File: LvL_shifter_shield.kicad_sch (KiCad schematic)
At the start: 10 parts, among them J1 Conn_02x08_Counter_Clockwise, J2 Conn_01x15_Socket, J3 Conn_01x15_Socket, J4 Power, U1 TXB0108DQSR, U2 TXB0108DQSR

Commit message: Updated silkscreen and added a +5 link to the nano
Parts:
- added R3: ${SIM.PARAMS}, Resistor_SMD:R_0603_1608Metric_Pad0.98x0.95mm_HandSolder, symbol Device:R_Small
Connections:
- net +5V: now also R3.2
- net +5V2: now also R3.1
- no-connect marks 11 -> 12
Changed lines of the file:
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@@
   (junction (at 53.34 119.38) (diameter 0) (color 0 0 0 0)
+  )
+  (junction (at 50.8 144.78) (diameter 0) (color 0 0 0 0)
+  )
+  (junction (at 106.68 20.32) (diameter 0) (color 0 0 0 0)
   )
   (junction (at 58.42 77.47) (diameter 0) (color 0 0 0 0)
@@
   (no_connect (at 77.47 147.32))
   (no_connect (at 77.47 139.7))
+  (no_connect (at 109.22 20.32))
   (no_connect (at 77.47 142.24))
   (wire (pts (xy 58.42 138.43) (xy 53.34 138.43))
@@
     (stroke (width 0) (type default))
   )
+  (wire (pts (xy 50.8 144.78) (xy 35.56 144.78))
+    (stroke (width 0) (type default))
+  )
   (wire (pts (xy 132.08 54.61) (xy 175.26 54.61))
     (stroke (width 0) (type default))
@@
     (stroke (width 0) (type default))
   )
+  (wire (pts (xy 35.56 144.78) (xy 35.56 16.51))
+    (stroke (width 0) (type default))
+  )
   (wire (pts (xy 157.48 64.77) (xy 175.26 64.77))
     (stroke (width 0) (type default))
@@
     (stroke (width 0) (type default))
   )
+  (wire (pts (xy 106.68 20.32) (xy 114.3 20.32))
+    (stroke (width 0) (type default))
+  )
   (wire (pts (xy 83.82 121.92) (xy 83.82 62.23))
     (stroke (width 0) (type default))
@@
     (stroke (width 0) (type default))
   )
+  (wire (pts (xy 104.14 15.24) (xy 104.14 16.51))
+    (stroke (width 0) (type default))
+  )
   (wire (pts (xy 101.6 25.4) (xy 101.6 74.93))
     (stroke (width 0) (type default))
@@
     (stroke (width 0) (type default))
   )
+  (wire (pts (xy 35.56 16.51) (xy 104.14 16.51))
+    (stroke (width 0) (type default))
+  )
   (wire (pts (xy 105.41 40.64) (xy 105.41 41.91))
     (stroke (width 0) (type default))
@@
     (stroke (width 0) (type default))
   )
-  (wire (pts (xy 101.6 20.32) (xy 114.3 20.32))
+  (wire (pts (xy 101.6 20.32) (xy 106.68 20.32))
     (stroke (width 0) (type default))
   )
@@
   )
   (wire (pts (xy 124.46 20.32) (xy 124.46 34.29))
+    (stroke (width 0) (type default))
+  )
+  (wire (pts (xy 106.68 15.24) (xy 104.14 15.24))
     (stroke (width 0) (type default))
   )
@@
         )
       )
+    )
+  )
+  (symbol (lib_id "Device:R_Small") (at 106.68 17.78 0) (unit 1)
+    (in_bom yes) (on_board yes) (dnp no) (fields_autoplaced)
+    (property "Reference" "R3" (at 109.22 16.51 0)
+      (effects (font (size 1.27 1.27)) (justify left))
+    )
+    (property "Value" "${SIM.PARAMS}" (at 109.22 19.05 0)
+      (effects (font (size 1.27 1.27)) (justify left))
+    )
+    (property "Footprint" "Resistor_SMD:R_0603_1608Metric_Pad0.98x0.95mm_HandSolder" (at 106.68 17.78 0)
+      (effects (font (size 1.27 1.27)) hide)
+    )
+    (property "Datasheet" "~" (at 106.68 17.78 0)
+      (effects (font (size 1.27 1.27)) hide)
+    )
+    (property "Sim.Device" "R" (at 106.68 17.78 0)
+      (effects (font (size 1.27 1.27)) hide)
+    )
+    (property "Sim.Type" "=" (at 106.68 17.78 0)
+      (effects (font (size 1.27 1.27)) hide)
+    )
+    (property "Sim.Params" "r=0" (at 106.68 17.78 0)
+      (effects (font (size 1.27 1.27)) hide)
+    )
+    (property "Sim.Pins" "1=+ 2=-" (at 106.68 17.78 0)
+      (effects (font (size 1.27 1.27)) hide)
+    )
+    (pin "1")
+    (pin "2")
+    (instances
+      (project "LvL_shifter_shield"
+        (path "/74ddfcee-fcec-4e00-880d-25eef1dc4f86"
+          (reference "R3") (unit 1)
+        )
+      )

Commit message: Forgot to set OE high when power is connected
You can work around this with a jumper wire from 3.3v to the OE side of the R1 and R2
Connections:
- net +3.3V: now also R1.2, R2.2, U1.6 (OE), U2.6 (OE)
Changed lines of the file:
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@@
 (kicad_sch (version 20230121) (generator eeschema)
   (paper "A4")
+  (junction (at 106.68 77.47) (diameter 0) (color 0 0 0 0)
+  )
   (junction (at 53.34 139.7) (diameter 0) (color 0 0 0 0)
   )
@@
   (junction (at 99.06 77.47) (diameter 0) (color 0 0 0 0)
   )
+  (junction (at 106.68 85.09) (diameter 0) (color 0 0 0 0)
+  )
   (junction (at 105.41 27.94) (diameter 0) (color 0 0 0 0)
   )
@@
   )
   (junction (at 50.8 144.78) (diameter 0) (color 0 0 0 0)
+  )
+  (junction (at 106.68 41.91) (diameter 0) (color 0 0 0 0)
   )
   (junction (at 106.68 20.32) (diameter 0) (color 0 0 0 0)
@@
     (stroke (width 0) (type default))
   )
+  (wire (pts (xy 106.68 41.91) (xy 106.68 77.47))
+    (stroke (width 0) (type default))
+  )
   (wire (pts (xy 157.48 64.77) (xy 175.26 64.77))
     (stroke (width 0) (type default))
@@
     (stroke (width 0) (type default))
   )
+  (wire (pts (xy 106.68 77.47) (xy 119.38 77.47))
+    (stroke (width 0) (type default))
+  )
   (wire (pts (xy 86.36 124.46) (xy 86.36 49.53))
     (stroke (width 0) (type default))
@@
     (stroke (width 0) (type default))
   )
-  (wire (pts (xy 105.41 41.91) (xy 111.76 41.91))
+  (wire (pts (xy 105.41 41.91) (xy 106.68 41.91))
     (stroke (width 0) (type default))
   )
@@
     (stroke (width 0) (type default))
   )
-  (wire (pts (xy 99.06 77.47) (xy 119.38 77.47))
+  (wire (pts (xy 99.06 77.47) (xy 106.68 77.47))
     (stroke (width 0) (type default))
   )
@@
     (stroke (width 0) (type default))
   )
+  (wire (pts (xy 106.68 41.91) (xy 111.76 41.91))
+    (stroke (width 0) (type default))
+  )
+  (wire (pts (xy 106.68 85.09) (xy 111.76 85.09))
+    (stroke (width 0) (type default))
+  )
   (wire (pts (xy 199.39 72.39) (xy 199.39 57.15))
     (stroke (width 0) (type default))
@@
     (stroke (width 0) (type default))
   )
+  (wire (pts (xy 104.14 85.09) (xy 106.68 85.09))
+    (stroke (width 0) (type default))
+  )
   (wire (pts (xy 40.64 129.54) (xy 40.64 97.79))
     (stroke (width 0) (type default))
@@
     (stroke (width 0) (type default))
   )
-  (wire (pts (xy 104.14 85.09) (xy 111.76 85.09))
-    (stroke (width 0) (type default))
-  )
   (wire (pts (xy 121.92 144.78) (xy 199.39 144.78))
     (stroke (width 0) (type default))
@@
     (stroke (width 0) (type default))
   )
+  (wire (pts (xy 106.68 77.47) (xy 106.68 85.09))
+    (stroke (width 0) (type default))
+  )

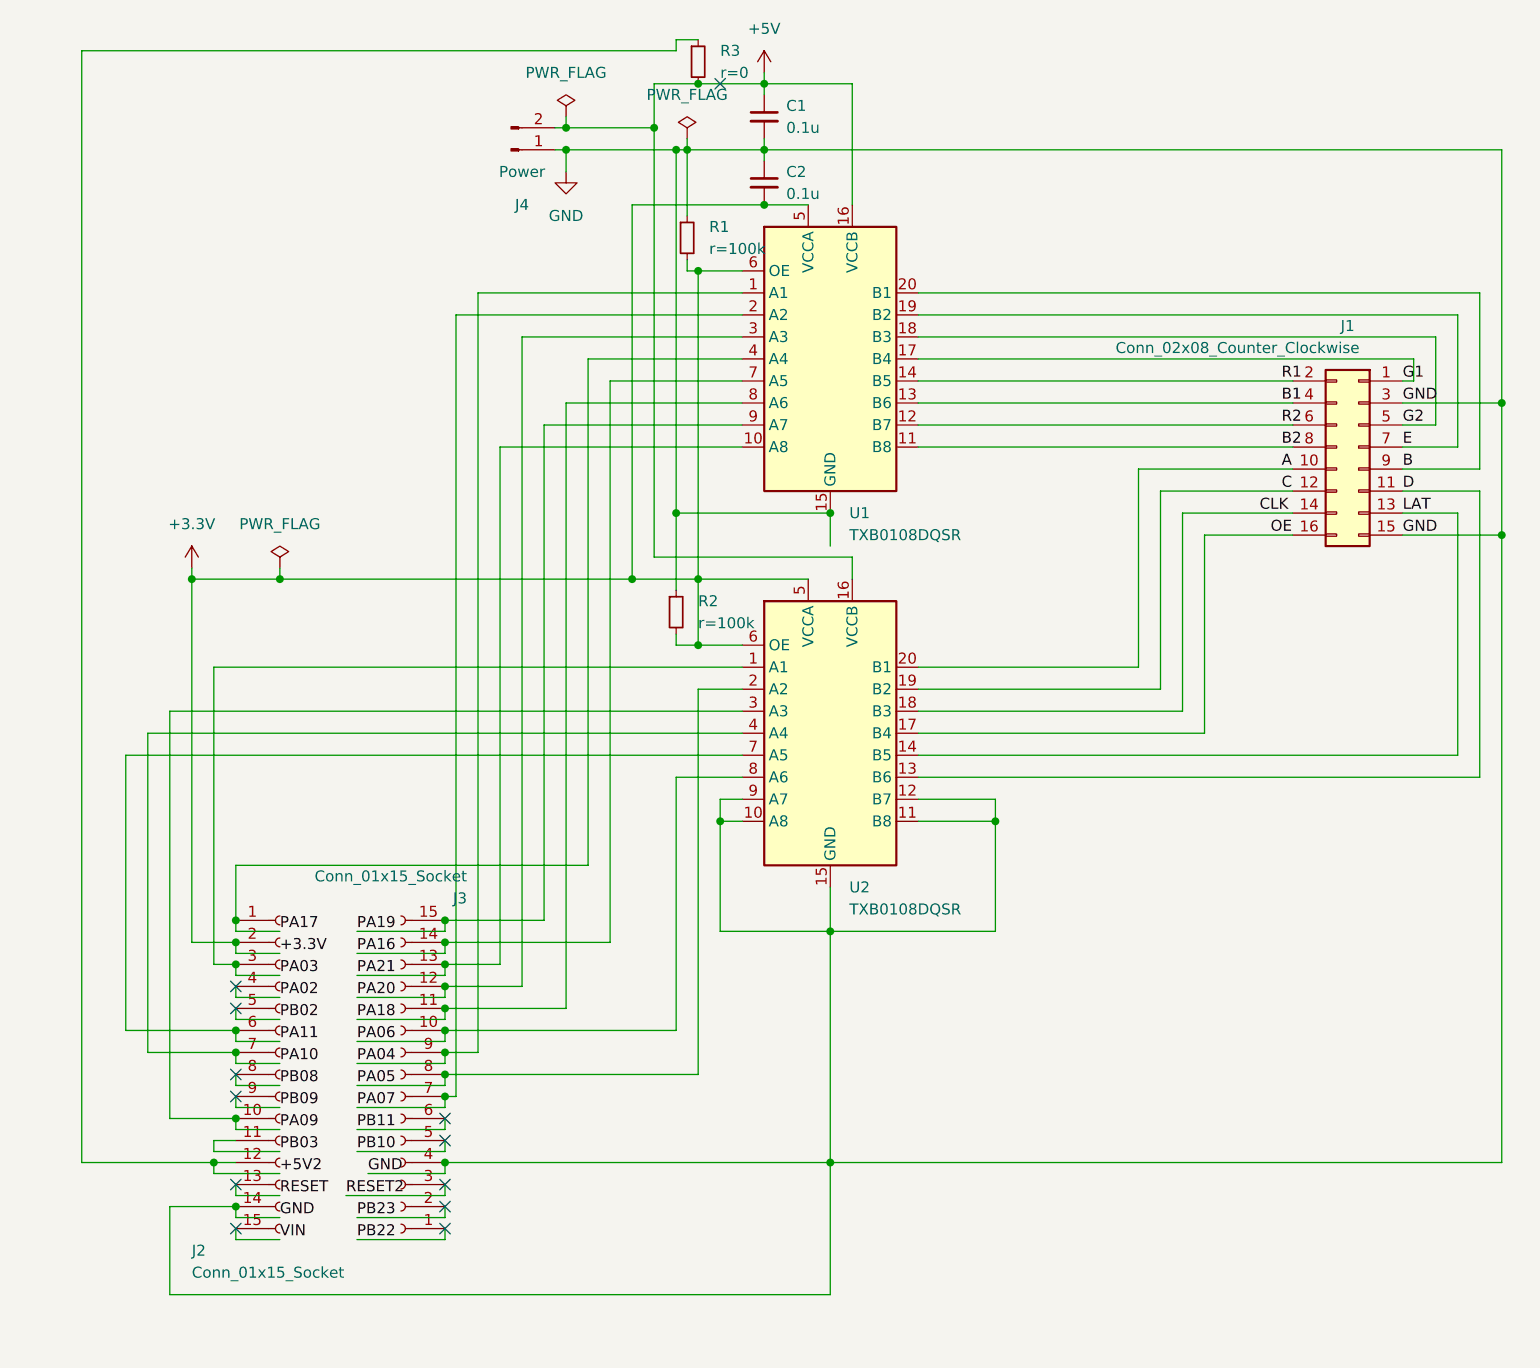
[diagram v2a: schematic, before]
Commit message: Updated version number, added open hardware logo
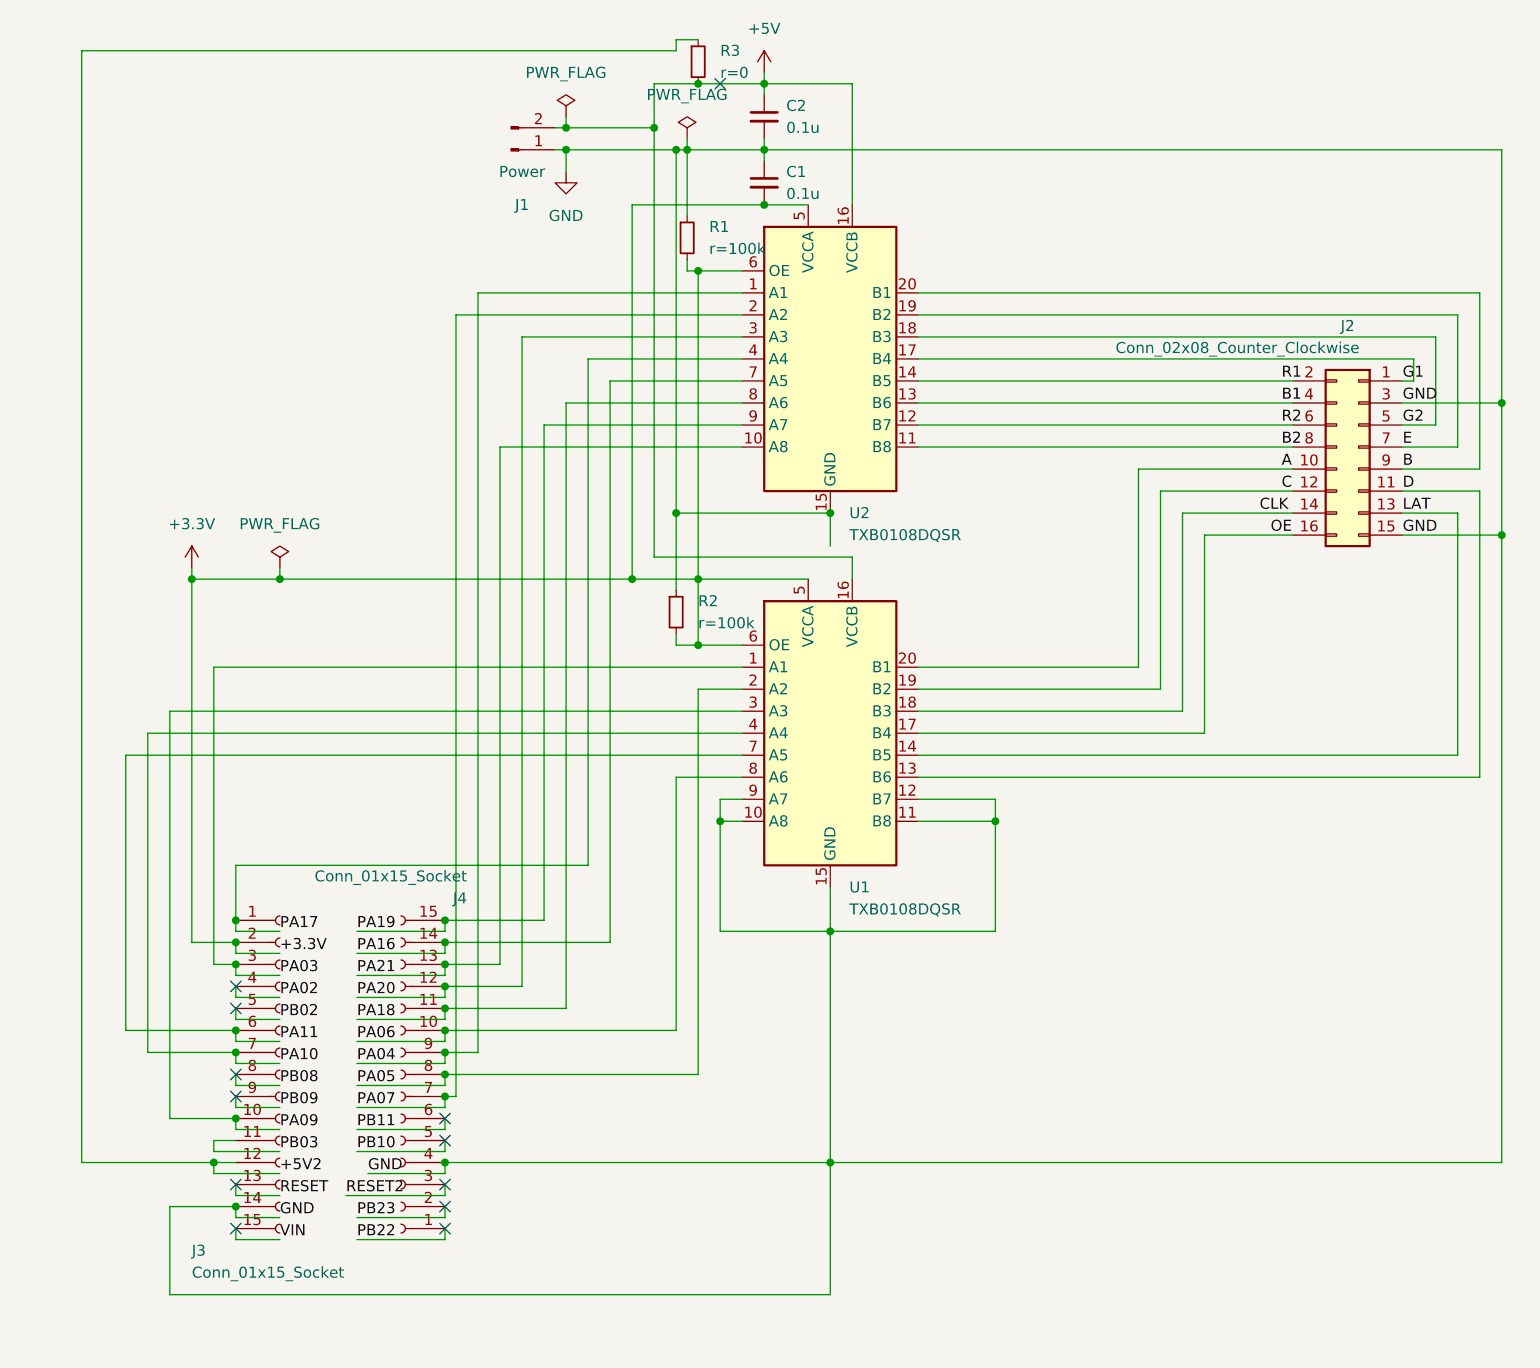
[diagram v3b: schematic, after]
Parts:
- R1, R2: value ${SIM.PARAMS} -> r=100k
- R3: value ${SIM.PARAMS} -> r=0
- renumbered C2 to C1, C1 to C2, J4 to J1, J1 to J2, J2 to J3, J3 to J4, U2 to U1, U1 to U2
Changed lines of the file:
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@@
   (symbol (lib_id "Logic_LevelTranslator:TXB0108DQSR") (at 121.92 95.25 0) (unit 1)
     (in_bom yes) (on_board yes) (dnp no) (fields_autoplaced)
-    (property "Reference" "U2" (at 124.1141 113.03 0)
+    (property "Reference" "U1" (at 124.1141 113.03 0)
       (effects (font (size 1.27 1.27)) (justify left))
     )
@@
       (project "LvL_shifter_shield"
         (path "/74ddfcee-fcec-4e00-880d-25eef1dc4f86"
-          (reference "U2") (unit 1)
+          (reference "U1") (unit 1)
         )
       )
@@
   (symbol (lib_id "Logic_LevelTranslator:TXB0108DQSR") (at 121.92 52.07 0) (unit 1)
     (in_bom yes) (on_board yes) (dnp no) (fields_autoplaced)
-    (property "Reference" "U1" (at 124.1141 69.85 0)
+    (property "Reference" "U2" (at 124.1141 69.85 0)
       (effects (font (size 1.27 1.27)) (justify left))
     )
@@
       (project "LvL_shifter_shield"
         (path "/74ddfcee-fcec-4e00-880d-25eef1dc4f86"
-          (reference "U1") (unit 1)
+          (reference "U2") (unit 1)
         )
       )
@@
   (symbol (lib_id "Connector_Generic:Conn_02x08_Odd_Even") (at 182.88 62.23 0) (mirror y) (unit 1)
     (in_bom yes) (on_board yes) (dnp no)
-    (property "Reference" "J1" (at 181.61 48.26 0)
+    (property "Reference" "J2" (at 181.61 48.26 0)
       (effects (font (size 1.27 1.27)))
     )
@@
       (project "LvL_shifter_shield"
         (path "/74ddfcee-fcec-4e00-880d-25eef1dc4f86"
-          (reference "J1") (unit 1)
+          (reference "J2") (unit 1)
         )
       )
@@
   (symbol (lib_id "Connector:Conn_01x15_Socket") (at 72.39 134.62 180) (unit 1)
     (in_bom yes) (on_board yes) (dnp no)
-    (property "Reference" "J3" (at 80.01 114.3 0)
+    (property "Reference" "J4" (at 80.01 114.3 0)
       (effects (font (size 1.27 1.27)) (justify left))
     )
@@
       (project "LvL_shifter_shield"
         (path "/74ddfcee-fcec-4e00-880d-25eef1dc4f86"
-          (reference "J3") (unit 1)
+          (reference "J4") (unit 1)
         )
       )
@@
       (effects (font (size 1.27 1.27)) (justify left))
     )
-    (property "Value" "${SIM.PARAMS}" (at 109.22 19.05 0)
+    (property "Value" "r=0" (at 109.22 19.05 0)
       (effects (font (size 1.27 1.27)) (justify left))
     )
@@
   (symbol (lib_id "Connector:Conn_01x02_Pin") (at 85.09 27.94 0) (mirror x) (unit 1)
     (in_bom yes) (on_board yes) (dnp no)
-    (property "Reference" "J4" (at 86.36 34.29 0)
+    (property "Reference" "J1" (at 86.36 34.29 0)
       (effects (font (size 1.27 1.27)))
     )
@@
       (project "LvL_shifter_shield"
         (path "/74ddfcee-fcec-4e00-880d-25eef1dc4f86"
-          (reference "J4") (unit 1)
+          (reference "J1") (unit 1)
         )
       )
@@
   (symbol (lib_id "Device:C_Small") (at 114.3 24.13 0) (unit 1)
     (in_bom yes) (on_board yes) (dnp no)
-    (property "Reference" "C1" (at 116.84 22.8663 0)
+    (property "Reference" "C2" (at 116.84 22.8663 0)
       (effects (font (size 1.27 1.27)) (justify left))
     )
@@
       (project "LvL_shifter_shield"
         (path "/74ddfcee-fcec-4e00-880d-25eef1dc4f86"
-          (reference "C1") (unit 1)
+          (reference "C2") (unit 1)
         )
       )
@@
       (effects (font (size 1.27 1.27)) (justify left))
     )
-    (property "Value" "${SIM.PARAMS}" (at 107.95 39.37 0)
+    (property "Value" "r=100k" (at 107.95 39.37 0)
       (effects (font (size 1.27 1.27)) (justify left))
     )
@@
       (effects (font (size 1.27 1.27)) (justify left))
     )
-    (property "Value" "${SIM.PARAMS}" (at 106.68 82.55 0)
+    (property "Value" "r=100k" (at 106.68 82.55 0)
       (effects (font (size 1.27 1.27)) (justify left))
     )
@@
   (symbol (lib_id "Device:C_Small") (at 114.3 31.75 0) (unit 1)
     (in_bom yes) (on_board yes) (dnp no)
-    (property "Reference" "C2" (at 116.84 30.4863 0)
+    (property "Reference" "C1" (at 116.84 30.4863 0)
       (effects (font (size 1.27 1.27)) (justify left))
     )
@@
       (project "LvL_shifter_shield"
         (path "/74ddfcee-fcec-4e00-880d-25eef1dc4f86"
-          (reference "C2") (unit 1)
+          (reference "C1") (unit 1)
         )
       )
@@
   (symbol (lib_id "Connector:Conn_01x15_Socket") (at 58.42 134.62 0) (unit 1)
     (in_bom yes) (on_board yes) (dnp no)
-    (property "Reference" "J2" (at 48.26 154.94 0)
+    (property "Reference" "J3" (at 48.26 154.94 0)
       (effects (font (size 1.27 1.27)) (justify left))
     )
@@
       (project "LvL_shifter_shield"
         (path "/74ddfcee-fcec-4e00-880d-25eef1dc4f86"
-          (reference "J2") (unit 1)
-        )
-      )
+          (reference "J3") (unit 1)
+        )
+      )
